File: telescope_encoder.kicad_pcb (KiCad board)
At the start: 2 copper layers, 9 parts, among them J1 Conn_01x04_Male, J2 Conn_01x02_Male, U1 AS5048B

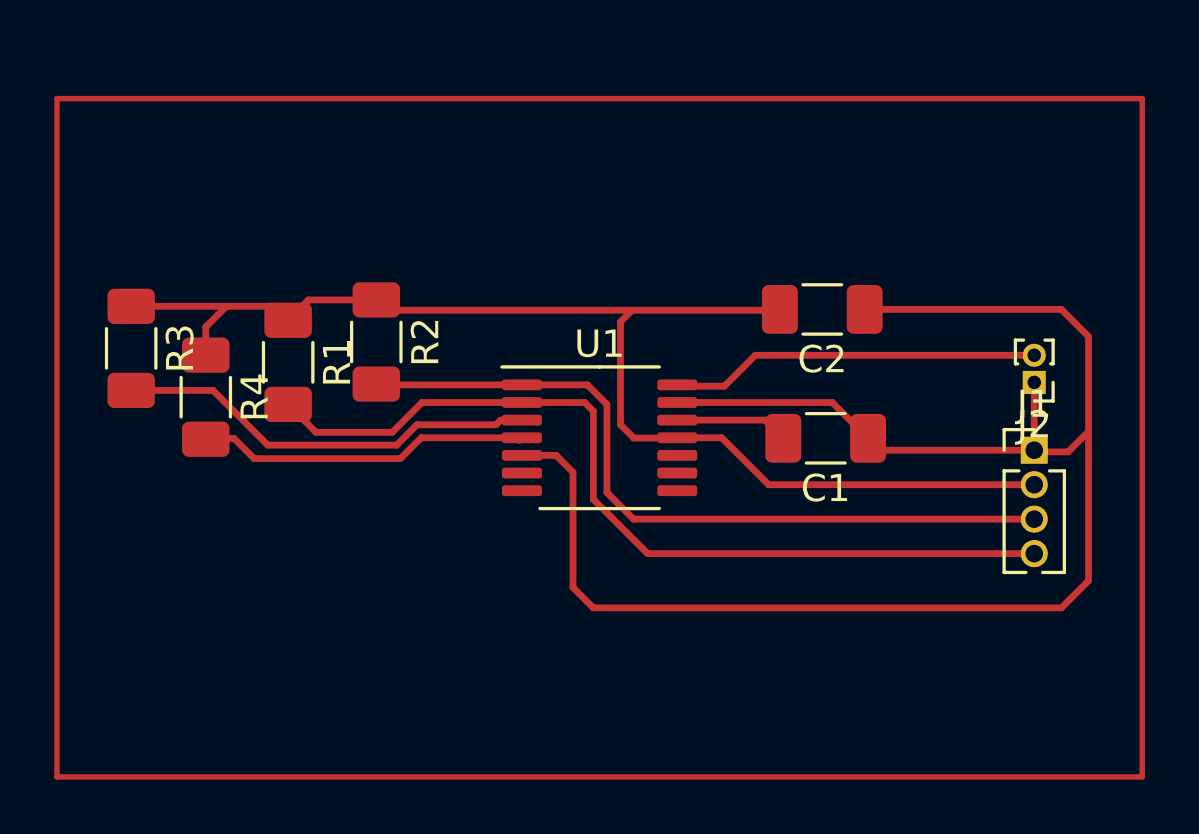
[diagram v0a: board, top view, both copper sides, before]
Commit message: Updated PCB
The tracks need to be checked for parasitic capacitance issues
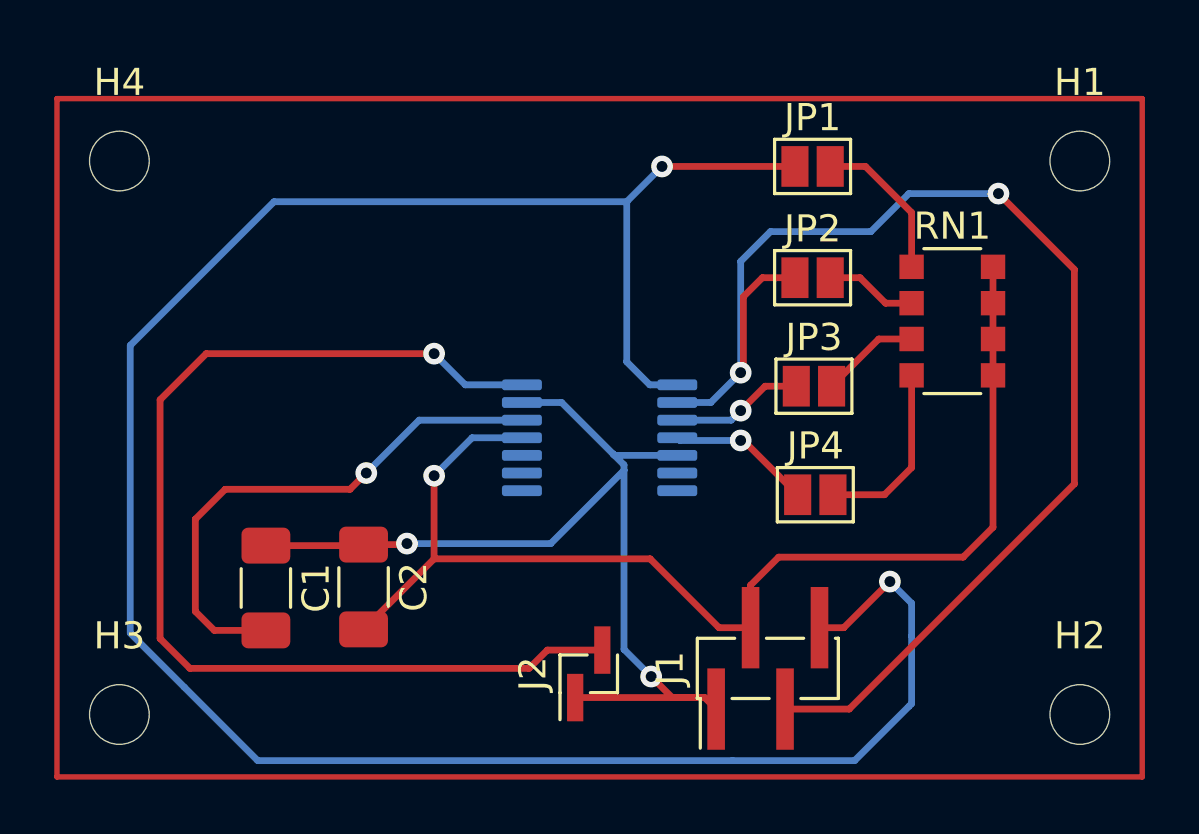
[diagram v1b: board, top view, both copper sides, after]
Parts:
- removed R1, R2, R3, R4: 10 kΩ, Resistor_SMD:R_1206_3216Metric_Pad1.30x1.75mm_HandSolder
- added H1: MountingHole, MountingHole:MountingHole_2.2mm_M2_DIN965, F.Cu at (174.7, 84.8)
- added H2: MountingHole, MountingHole:MountingHole_2.2mm_M2_DIN965, F.Cu at (174.7, 105.2)
- added H3: MountingHole, MountingHole:MountingHole_2.2mm_M2_DIN965, F.Cu at (139.3, 105.2)
- added H4: MountingHole, MountingHole:MountingHole_2.2mm_M2_DIN965, F.Cu at (139.3, 84.8)
- added JP1: SolderJumper_2_Open, Jumper:SolderJumper-2_P1.3mm_Open_Pad1.0x1.5mm, F.Cu at (164.8, 85.0)
- added JP2: SolderJumper_2_Open, Jumper:SolderJumper-2_P1.3mm_Open_Pad1.0x1.5mm, F.Cu at (164.8, 89.1)
- added JP3: SolderJumper_2_Open, Jumper:SolderJumper-2_P1.3mm_Open_Pad1.0x1.5mm, F.Cu at (164.9, 93.1)
- added JP4: SolderJumper_2_Open, Jumper:SolderJumper-2_P1.3mm_Open_Pad1.0x1.5mm, F.Cu at (164.9, 97.1)
- added RN1: 10 kΩ, Resistor_SMD:R_Array_Convex_4x1206, F.Cu at (170.0, 90.7)
- J1: footprint Connector_PinHeader_1.27mm:PinHeader_1x04_P1.27mm_Vertical -> Connector_PinHeader_1.27mm:PinHeader_1x04_P1.27mm_Vertical_SMD_Pin1Left
- J2: footprint Connector_PinHeader_1.00mm:PinHeader_1x02_P1.00mm_Vertical -> Connector_PinHeader_1.00mm:PinHeader_1x02_P1.00mm_Vertical_SMD_Pin1Left
- U1: moved to B.Cu
- moved C1 21.4 mm to (144.7, 100.5), turned to -90 degrees
- moved C2 19.8 mm to (148.3, 100.5), turned to -90 degrees
- moved J2 19.6 mm to (156.6, 103.7), turned to 90 degrees
- moved J1 12.7 mm to (163.2, 103.5), turned to 90 degrees
- turned U1 to 180 degrees
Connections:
- J1 pad 3: Net-(U1-Pad1) -> Net-(J1-Pad3)
- J1 pad 4: Net-(U1-Pad2) -> Net-(J1-Pad4)
- U1 pad 1: Net-(U1-Pad1) -> Net-(J1-Pad4)
- U1 pad 2: Net-(U1-Pad2) -> Net-(J1-Pad3)
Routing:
- net Net-(J1-Pad4): track 0.00 -> 85.7 mm, vias 0 -> 2
- net Net-(J1-Pad3): track 0.00 -> 48.4 mm, vias 0 -> 2
- net Net-(U1-Pad2): track 32.6 -> 0.00 mm
- net Net-(U1-Pad1): track 28.3 -> 0.00 mm
- net Net-(J2-Pad2): track 13.7 -> 40.4 mm, vias 0 -> 1
- net GND: track 63.0 -> 37.3 mm, vias 0 -> 2
- net Net-(C1-Pad2): track 4.19 -> 19.8 mm, vias 0 -> 1
- net Net-(JP3-Pad1): track 15.6 -> 4.91 mm, vias 0 -> 1
- net Net-(JP4-Pad1): track 12.6 -> 5.31 mm, vias 0 -> 1
- net Net-(JP4-Pad2): track 0.00 -> 6.71 mm
- net Net-(JP1-Pad2): track 0.00 -> 5.70 mm
- net Net-(JP3-Pad2): track 0.00 -> 3.67 mm
- net Net-(JP2-Pad2): track 0.00 -> 3.39 mm
- net +5V: track 47.3 -> 44.3 mm, vias 0 -> 1
